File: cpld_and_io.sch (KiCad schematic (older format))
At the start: 3 parts, among them U12 IS61LV5128AL-10TLI, U4 5M1270ZT144C5N

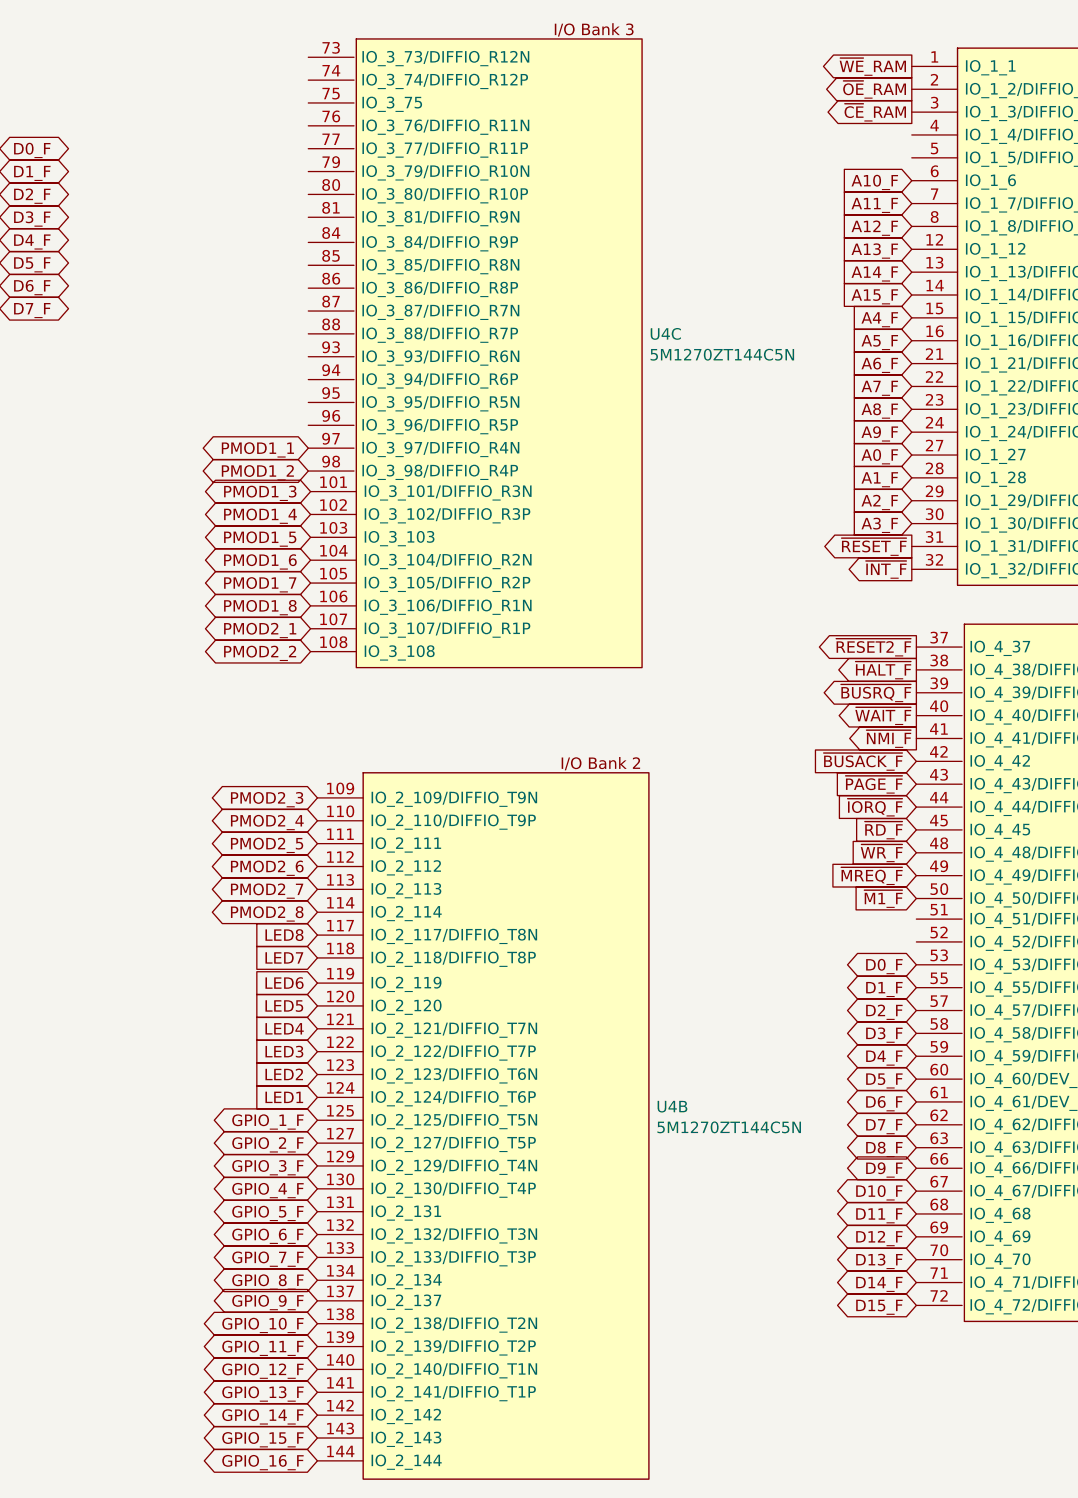
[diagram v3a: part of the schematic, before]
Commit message: organized bypass caps
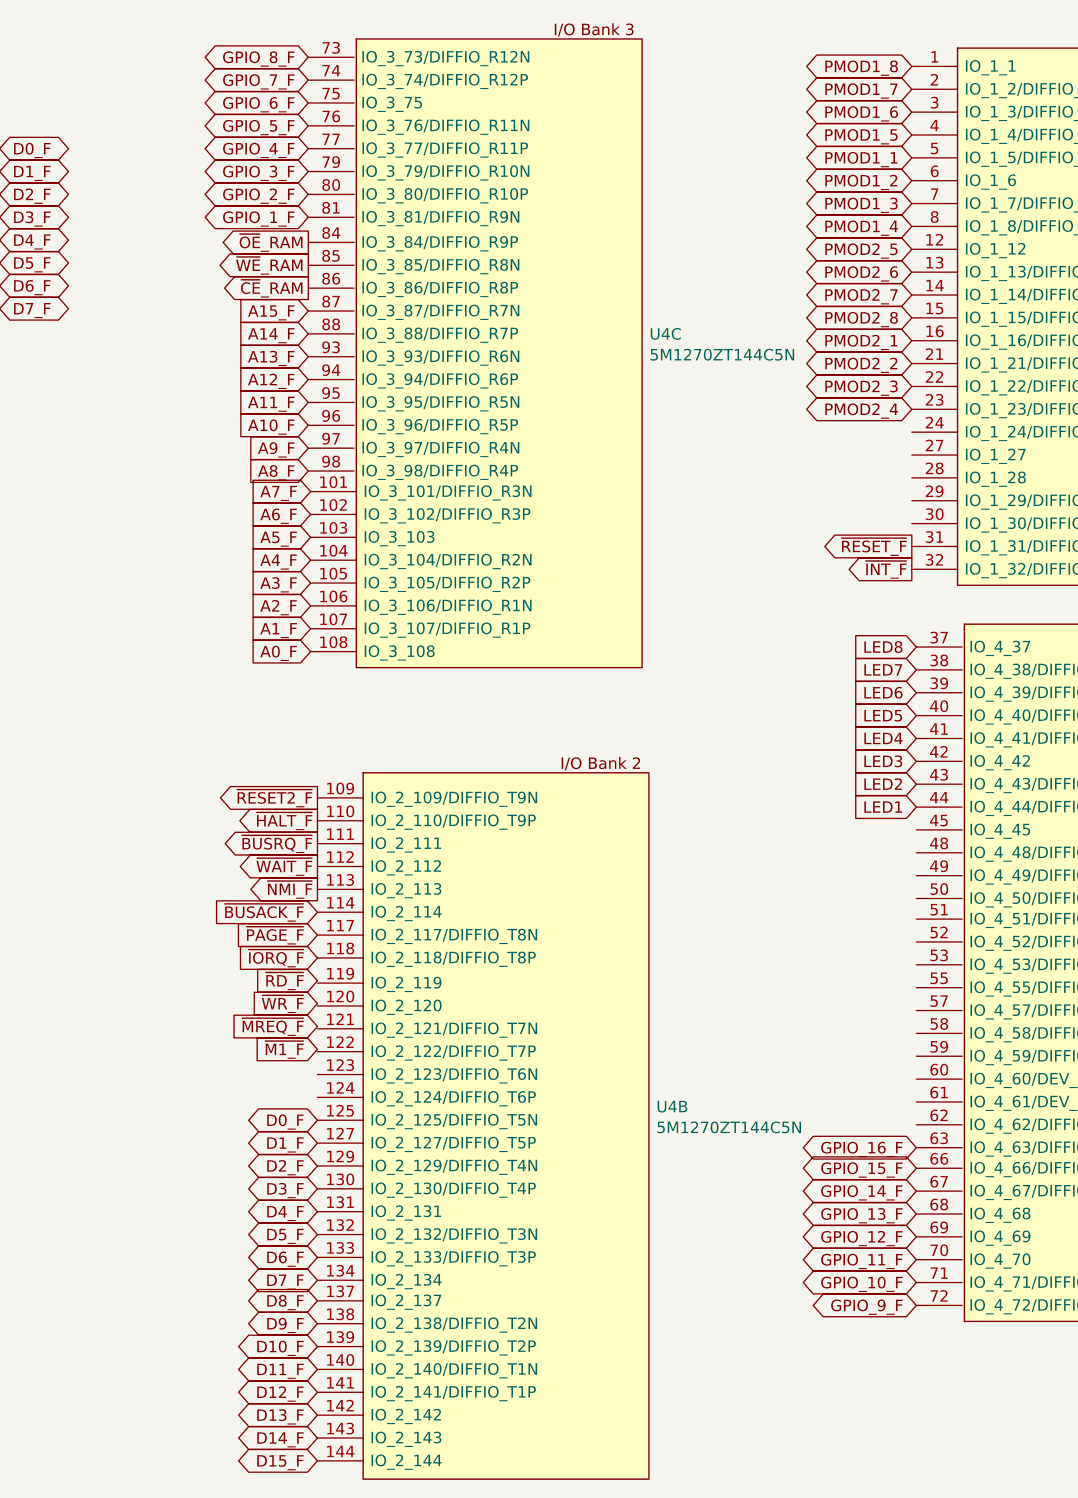
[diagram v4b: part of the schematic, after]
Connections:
- net A0_F: now also U4.108 (IO_3_108); no longer U4.27 (IO_1_27)
- net A10_F: now also U4.96 (IO_3_96/DIFFIO_R5P); no longer U4.6 (IO_1_6)
- net A11_F: now also U4.95 (IO_3_95/DIFFIO_R5N); no longer U4.7 (IO_1_7/DIFFIO_L3P)
- net A12_F: now also U4.94 (IO_3_94/DIFFIO_R6P); no longer U4.8 (IO_1_8/DIFFIO_L3N)
- net A13_F: now also U4.93 (IO_3_93/DIFFIO_R6N); no longer U4.12 (IO_1_12)
- net A14_F: now also U4.88 (IO_3_88/DIFFIO_R7P); no longer U4.13 (IO_1_13/DIFFIO_L4P)
- net A15_F: now also U4.87 (IO_3_87/DIFFIO_R7N); no longer U4.14 (IO_1_14/DIFFIO_L4N)
- net A1_F: now also U4.107 (IO_3_107/DIFFIO_R1P); no longer U4.28 (IO_1_28)
- net A2_F: now also U4.106 (IO_3_106/DIFFIO_R1N); no longer U4.29 (IO_1_29/DIFFIO_L8P)
- net A3_F: now also U4.105 (IO_3_105/DIFFIO_R2P); no longer U4.30 (IO_1_30/DIFFIO_L8N)
- net A4_F: now also U4.104 (IO_3_104/DIFFIO_R2N); no longer U4.15 (IO_1_15/DIFFIO_L5P)
- net A5_F: now also U4.103 (IO_3_103); no longer U4.16 (IO_1_16/DIFFIO_L5N)
- net A6_F: now also U4.102 (IO_3_102/DIFFIO_R3P); no longer U4.21 (IO_1_21/DIFFIO_L6P)
- net A7_F: now also U4.101 (IO_3_101/DIFFIO_R3N); no longer U4.22 (IO_1_22/DIFFIO_L6N)
- net A8_F: now also U4.98 (IO_3_98/DIFFIO_R4P); no longer U4.23 (IO_1_23/DIFFIO_L7P)
- net A9_F: now also U4.97 (IO_3_97/DIFFIO_R4N); no longer U4.24 (IO_1_24/DIFFIO_L7N)
- net D0_F: now also U4.125 (IO_2_125/DIFFIO_T5N); no longer U4.53 (IO_4_53/DIFFIO_B6N)
- net D10_F: now also U4.139 (IO_2_139/DIFFIO_T2P); no longer U4.67 (IO_4_67/DIFFIO_B11N)
- net D11_F: now also U4.140 (IO_2_140/DIFFIO_T1N); no longer U4.68 (IO_4_68)
- net D12_F: now also U4.141 (IO_2_141/DIFFIO_T1P); no longer U4.69 (IO_4_69)
- net D13_F: now also U4.142 (IO_2_142); no longer U4.70 (IO_4_70)
- net D14_F: now also U4.143 (IO_2_143); no longer U4.71 (IO_4_71/DIFFIO_B12P)
- net D15_F: now also U4.144 (IO_2_144); no longer U4.72 (IO_4_72/DIFFIO_B12N)
- net D1_F: now also U4.127 (IO_2_127/DIFFIO_T5P); no longer U4.55 (IO_4_55/DIFFIO_B7P)
- net D2_F: now also U4.129 (IO_2_129/DIFFIO_T4N); no longer U4.57 (IO_4_57/DIFFIO_B7N)
- net D3_F: now also U4.130 (IO_2_130/DIFFIO_T4P); no longer U4.58 (IO_4_58/DIFFIO_B8P)
- net D4_F: now also U4.131 (IO_2_131); no longer U4.59 (IO_4_59/DIFFIO_B8N)
- net D5_F: now also U4.132 (IO_2_132/DIFFIO_T3N); no longer U4.60 (IO_4_60/DEV_OE/DIFFIO_B9P)
- net D6_F: now also U4.133 (IO_2_133/DIFFIO_T3P); no longer U4.61 (IO_4_61/DEV_CLRN/DIFFIO_B9N)
- net D7_F: now also U4.134 (IO_2_134); no longer U4.62 (IO_4_62/DIFFIO_B10P)
- net D8_F: now also U4.137 (IO_2_137); no longer U4.63 (IO_4_63/DIFFIO_B10N)
- net D9_F: now also U4.138 (IO_2_138/DIFFIO_T2N); no longer U4.66 (IO_4_66/DIFFIO_B11P)
- net GPIO_10_F: now also U4.71 (IO_4_71/DIFFIO_B12P); no longer U4.138 (IO_2_138/DIFFIO_T2N)
- net GPIO_11_F: now also U4.70 (IO_4_70); no longer U4.139 (IO_2_139/DIFFIO_T2P)
- net GPIO_12_F: now also U4.69 (IO_4_69); no longer U4.140 (IO_2_140/DIFFIO_T1N)
- net GPIO_13_F: now also U4.68 (IO_4_68); no longer U4.141 (IO_2_141/DIFFIO_T1P)
- net GPIO_14_F: now also U4.67 (IO_4_67/DIFFIO_B11N); no longer U4.142 (IO_2_142)
- net GPIO_15_F: now also U4.66 (IO_4_66/DIFFIO_B11P); no longer U4.143 (IO_2_143)
- net GPIO_16_F: now also U4.63 (IO_4_63/DIFFIO_B10N); no longer U4.144 (IO_2_144)
- net GPIO_1_F: now also U4.81 (IO_3_81/DIFFIO_R9N); no longer U4.125 (IO_2_125/DIFFIO_T5N)
- net GPIO_2_F: now also U4.80 (IO_3_80/DIFFIO_R10P); no longer U4.127 (IO_2_127/DIFFIO_T5P)
- net GPIO_3_F: now also U4.79 (IO_3_79/DIFFIO_R10N); no longer U4.129 (IO_2_129/DIFFIO_T4N)
- net GPIO_4_F: now also U4.77 (IO_3_77/DIFFIO_R11P); no longer U4.130 (IO_2_130/DIFFIO_T4P)
- net GPIO_5_F: now also U4.76 (IO_3_76/DIFFIO_R11N); no longer U4.131 (IO_2_131)
- net GPIO_6_F: now also U4.75 (IO_3_75); no longer U4.132 (IO_2_132/DIFFIO_T3N)
- net GPIO_7_F: now also U4.74 (IO_3_74/DIFFIO_R12P); no longer U4.133 (IO_2_133/DIFFIO_T3P)
- net GPIO_8_F: now also U4.73 (IO_3_73/DIFFIO_R12N); no longer U4.134 (IO_2_134)
- net GPIO_9_F: now also U4.72 (IO_4_72/DIFFIO_B12N); no longer U4.137 (IO_2_137)
- net LED1: now also U4.44 (IO_4_44/DIFFIO_B3N); no longer U4.124 (IO_2_124/DIFFIO_T6P)
- net LED2: now also U4.43 (IO_4_43/DIFFIO_B3P); no longer U4.123 (IO_2_123/DIFFIO_T6N)
- net LED3: now also U4.42 (IO_4_42); no longer U4.122 (IO_2_122/DIFFIO_T7P)
- net LED4: now also U4.41 (IO_4_41/DIFFIO_B2N); no longer U4.121 (IO_2_121/DIFFIO_T7N)
- net LED5: now also U4.40 (IO_4_40/DIFFIO_B2P); no longer U4.120 (IO_2_120)
- net LED6: now also U4.39 (IO_4_39/DIFFIO_B1N); no longer U4.119 (IO_2_119)
- net LED7: now also U4.38 (IO_4_38/DIFFIO_B1P); no longer U4.118 (IO_2_118/DIFFIO_T8P)
- net LED8: now also U4.37 (IO_4_37); no longer U4.117 (IO_2_117/DIFFIO_T8N)
- net PMOD1_1: now also U4.5 (IO_1_5/DIFFIO_L2N); no longer U4.97 (IO_3_97/DIFFIO_R4N)
- net PMOD1_2: now also U4.6 (IO_1_6); no longer U4.98 (IO_3_98/DIFFIO_R4P)
- net PMOD1_3: now also U4.7 (IO_1_7/DIFFIO_L3P); no longer U4.101 (IO_3_101/DIFFIO_R3N)
- net PMOD1_4: now also U4.8 (IO_1_8/DIFFIO_L3N); no longer U4.102 (IO_3_102/DIFFIO_R3P)
- net PMOD1_5: now also U4.4 (IO_1_4/DIFFIO_L2P); no longer U4.103 (IO_3_103)
- net PMOD1_6: now also U4.3 (IO_1_3/DIFFIO_L1N); no longer U4.104 (IO_3_104/DIFFIO_R2N)
- net PMOD1_7: now also U4.2 (IO_1_2/DIFFIO_L1P); no longer U4.105 (IO_3_105/DIFFIO_R2P)
- net PMOD1_8: now also U4.1 (IO_1_1); no longer U4.106 (IO_3_106/DIFFIO_R1N)
- net PMOD2_1: now also U4.16 (IO_1_16/DIFFIO_L5N); no longer U4.107 (IO_3_107/DIFFIO_R1P)
- net PMOD2_2: now also U4.21 (IO_1_21/DIFFIO_L6P); no longer U4.108 (IO_3_108)
- net PMOD2_3: now also U4.22 (IO_1_22/DIFFIO_L6N); no longer U4.109 (IO_2_109/DIFFIO_T9N)
- net PMOD2_4: now also U4.23 (IO_1_23/DIFFIO_L7P); no longer U4.110 (IO_2_110/DIFFIO_T9P)
- net PMOD2_5: now also U4.12 (IO_1_12); no longer U4.111 (IO_2_111)
- net PMOD2_6: now also U4.13 (IO_1_13/DIFFIO_L4P); no longer U4.112 (IO_2_112)
- net PMOD2_7: now also U4.14 (IO_1_14/DIFFIO_L4N); no longer U4.113 (IO_2_113)
- net PMOD2_8: now also U4.15 (IO_1_15/DIFFIO_L5P); no longer U4.114 (IO_2_114)
- net ~BUSACK_F: now also U4.114 (IO_2_114); no longer U4.42 (IO_4_42)
- net ~BUSRQ_F: now also U4.111 (IO_2_111); no longer U4.39 (IO_4_39/DIFFIO_B1N)
- net ~CE~_RAM: now also U4.86 (IO_3_86/DIFFIO_R8P); no longer U4.3 (IO_1_3/DIFFIO_L1N)
- net ~HALT_F: now also U4.110 (IO_2_110/DIFFIO_T9P); no longer U4.38 (IO_4_38/DIFFIO_B1P)
- net ~IORQ_F: now also U4.118 (IO_2_118/DIFFIO_T8P); no longer U4.44 (IO_4_44/DIFFIO_B3N)
- net ~M1_F: no longer U4.50 (IO_4_50/DIFFIO_B5P)
- net ~MREQ_F: no longer U4.49 (IO_4_49/DIFFIO_B4N)
- net ~NMI_F: now also U4.113 (IO_2_113); no longer U4.41 (IO_4_41/DIFFIO_B2N)
- net ~OE~_RAM: now also U4.84 (IO_3_84/DIFFIO_R9P); no longer U4.2 (IO_1_2/DIFFIO_L1P)
- net ~PAGE_F: now also U4.117 (IO_2_117/DIFFIO_T8N); no longer U4.43 (IO_4_43/DIFFIO_B3P)
- net ~RD_F: no longer U4.45 (IO_4_45)
- net ~RESET2_F: now also U4.109 (IO_2_109/DIFFIO_T9N); no longer U4.37 (IO_4_37)
- net ~WAIT_F: now also U4.112 (IO_2_112); no longer U4.40 (IO_4_40/DIFFIO_B2P)
- net ~WE~_RAM: now also U4.85 (IO_3_85/DIFFIO_R8N); no longer U4.1 (IO_1_1)
- net ~WR_F: no longer U4.48 (IO_4_48/DIFFIO_B4P)
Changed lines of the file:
@@
 NoConn ~ 1830 2850
 NoConn ~ 1830 2950
-Text GLabel 7020 1490 0    50   Input ~ 0
-A12_F
-Text GLabel 7020 1590 0    50   Input ~ 0
-A13_F
-Text GLabel 7020 1690 0    50   Input ~ 0
-A14_F
-Text GLabel 7020 1790 0    50   Input ~ 0
-A15_F
-Text GLabel 7020 1390 0    50   Input ~ 0
-A11_F
-Text GLabel 7020 1290 0    50   Input ~ 0
-A10_F
-Text GLabel 7020 2390 0    50   Input ~ 0
+Text GLabel 4380 2460 0    50   Input ~ 0
 A9_F
-Text GLabel 7020 2290 0    50   Input ~ 0
+Text GLabel 4380 2560 0    50   Input ~ 0
 A8_F
-Text GLabel 7020 2190 0    50   Input ~ 0
+Text GLabel 4390 2650 0    50   Input ~ 0
 A7_F
-Text GLabel 7020 2090 0    50   Input ~ 0
+Text GLabel 4390 2750 0    50   Input ~ 0
 A6_F
-Text GLabel 7020 1990 0    50   Input ~ 0
+Text GLabel 4390 2850 0    50   Input ~ 0
 A5_F
-Text GLabel 7020 1890 0    50   Input ~ 0
+Text GLabel 4390 2950 0    50   Input ~ 0
 A4_F
-Text GLabel 7020 2790 0    50   Input ~ 0
+Text GLabel 4390 3050 0    50   Input ~ 0
 A3_F
-Text GLabel 7020 2690 0    50   Input ~ 0
+Text GLabel 4390 3150 0    50   Input ~ 0
 A2_F
-Text GLabel 7020 2590 0    50   Input ~ 0
+Text GLabel 4390 3250 0    50   Input ~ 0
 A1_F
-Text GLabel 7020 2490 0    50   Input ~ 0
+Text GLabel 4390 3350 0    50   Input ~ 0
 A0_F
-Text GLabel 7040 5420 0    50   3State ~ 0
+Text GLabel 4420 6100 0    50   3State ~ 0
 D7_F
-Text GLabel 7040 5320 0    50   3State ~ 0
+Text GLabel 4420 6000 0    50   3State ~ 0
 D6_F
-Text GLabel 7040 5220 0    50   3State ~ 0
+Text GLabel 4420 5900 0    50   3State ~ 0
 D5_F
-Text GLabel 7040 5120 0    50   3State ~ 0
+Text GLabel 4420 5800 0    50   3State ~ 0
 D4_F
-Text GLabel 7040 5020 0    50   3State ~ 0
+Text GLabel 4420 5700 0    50   3State ~ 0
 D3_F
-Text GLabel 7040 4920 0    50   3State ~ 0
+Text GLabel 4420 5600 0    50   3State ~ 0
 D2_F
-Text GLabel 7040 4820 0    50   3State ~ 0
+Text GLabel 4420 5500 0    50   3State ~ 0
 D1_F
-Text GLabel 7040 4720 0    50   3State ~ 0
+Text GLabel 4420 5400 0    50   3State ~ 0
 D0_F
-Text GLabel 7040 3830 0    50   Input ~ 0
+Text GLabel 4420 4490 0    50   Input ~ 0
 ~BUSACK_F
-Text GLabel 7040 3930 0    50   Input ~ 0
+Text GLabel 4420 4590 0    50   Input ~ 0
 ~PAGE_F
-Text GLabel 7040 4330 0    50   Input ~ 0
+Text GLabel 4420 4990 0    50   Input ~ 0
 ~MREQ_F
-Text GLabel 7040 4230 0    50   Input ~ 0
+Text GLabel 4420 4890 0    50   Input ~ 0
 ~WR_F
-Text GLabel 7040 4130 0    50   Input ~ 0
+Text GLabel 4420 4790 0    50   Input ~ 0
 ~RD_F
-Text GLabel 7040 4030 0    50   Input ~ 0
+Text GLabel 4420 4690 0    50   Input ~ 0
 ~IORQ_F
-Text GLabel 7040 4430 0    50   Input ~ 0
+Text GLabel 4420 5090 0    50   Input ~ 0
 ~M1_F
-Text GLabel 7040 3430 0    50   Output ~ 0
+Text GLabel 4420 4090 0    50   Output ~ 0
 ~HALT_F
-Text GLabel 7040 3530 0    50   Output ~ 0
+Text GLabel 4420 4190 0    50   Output ~ 0
 ~BUSRQ_F
-Text GLabel 7040 3630 0    50   Output ~ 0
+Text GLabel 4420 4290 0    50   Output ~ 0
 ~WAIT_F
-Text GLabel 7040 3730 0    50   Output ~ 0
+Text GLabel 4420 4390 0    50   Output ~ 0
 ~NMI_F
-Text GLabel 7040 3330 0    50   Output ~ 0
+Text GLabel 4420 3990 0    50   Output ~ 0
 ~RESET2_F
 Text GLabel 7020 2990 0    50   Output ~ 0
@@
 Text GLabel 7020 2890 0    50   Output ~ 0
 ~RESET_F
-Text GLabel 7040 6210 0    50   3State ~ 0
+Text GLabel 4420 6890 0    50   3State ~ 0
 D15_F
-Text GLabel 7040 6110 0    50   3State ~ 0
+Text GLabel 4420 6790 0    50   3State ~ 0
 D14_F
-Text GLabel 7040 6010 0    50   3State ~ 0
+Text GLabel 4420 6690 0    50   3State ~ 0
 D13_F
-Text GLabel 7040 5910 0    50   3State ~ 0
+Text GLabel 4420 6590 0    50   3State ~ 0
 D12_F
-Text GLabel 7040 5810 0    50   3State ~ 0
+Text GLabel 4420 6490 0    50   3State ~ 0
 D11_F
-Text GLabel 7040 5710 0    50   3State ~ 0
+Text GLabel 4420 6390 0    50   3State ~ 0
 D10_F
-Text GLabel 7040 5610 0    50   3State ~ 0
+Text GLabel 4420 6290 0    50   3State ~ 0
 D9_F
-Text GLabel 7040 5520 0    50   3State ~ 0
+Text GLabel 4420 6190 0    50   3State ~ 0
 D8_F
-Text GLabel 7020 790  0    50   Output ~ 0
-~WE~_RAM
-Text GLabel 7020 890  0    50   Output ~ 0
-~OE~_RAM
-Text GLabel 7020 990  0    50   Output ~ 0
+Text GLabel 4380 1760 0    50   Output ~ 0
 ~CE~_RAM
 $Comp
@@
 	1    0    0    -1
 $EndComp
-Text GLabel 4420 6100 0    50   3State ~ 0
-GPIO_8_F
-Text GLabel 4420 6000 0    50   3State ~ 0
-GPIO_7_F
-Text GLabel 4420 5900 0    50   3State ~ 0
-GPIO_6_F
-Text GLabel 4420 5800 0    50   3State ~ 0
-GPIO_5_F
-Text GLabel 4420 5700 0    50   3State ~ 0
-GPIO_4_F
-Text GLabel 4420 5600 0    50   3State ~ 0
-GPIO_3_F
-Text GLabel 4420 5500 0    50   3State ~ 0
-GPIO_2_F
-Text GLabel 4420 5400 0    50   3State ~ 0
-GPIO_1_F
-Text GLabel 4420 6890 0    50   3State ~ 0
-GPIO_16_F
-Text GLabel 4420 6790 0    50   3State ~ 0
-GPIO_15_F
-Text GLabel 4420 6690 0    50   3State ~ 0
-GPIO_14_F
-Text GLabel 4420 6590 0    50   3State ~ 0
-GPIO_13_F
-Text GLabel 4420 6490 0    50   3State ~ 0
-GPIO_12_F
-Text GLabel 4420 6390 0    50   3State ~ 0
-GPIO_11_F
-Text GLabel 4420 6290 0    50   3State ~ 0
+Text GLabel 7040 6110 0    50   3State ~ 0
 GPIO_10_F
-Text GLabel 4420 6190 0    50   3State ~ 0
+Text GLabel 7040 6210 0    50   3State ~ 0
 GPIO_9_F
 Text GLabel 1000 3250 0    50   Input ~ 0
@@
 	1310 3350 1000 3350
 NoConn ~ 1410 2980
-Text GLabel 4380 2460 0    50   3State ~ 0
+Text GLabel 7020 1190 0    50   3State ~ 0
 PMOD1_1
-Text GLabel 4380 2560 0    50   3State ~ 0
+Text GLabel 7020 1290 0    50   3State ~ 0
 PMOD1_2
-Text GLabel 4390 2650 0    50   3State ~ 0
+Text GLabel 7020 1390 0    50   3State ~ 0
 PMOD1_3
-Text GLabel 4390 2750 0    50   3State ~ 0
+Text GLabel 7020 1490 0    50   3State ~ 0
 PMOD1_4
-Text GLabel 4390 2850 0    50   3State ~ 0
+Text GLabel 7020 1090 0    50   3State ~ 0
 PMOD1_5
-Text GLabel 4390 2950 0    50   3State ~ 0
+Text GLabel 7020 990  0    50   3State ~ 0
 PMOD1_6
-Text GLabel 4390 3050 0    50   3State ~ 0
+Text GLabel 7020 890  0    50   3State ~ 0
 PMOD1_7
-Text GLabel 4390 3150 0    50   3State ~ 0
+Text GLabel 7020 790  0    50   3State ~ 0
 PMOD1_8
-Text GLabel 4390 3250 0    50   3State ~ 0
+Text GLabel 7020 1990 0    50   3State ~ 0
 PMOD2_1
-Text GLabel 4390 3350 0    50   3State ~ 0
+Text GLabel 7020 2090 0    50   3State ~ 0
 PMOD2_2
-Text GLabel 4420 3990 0    50   3State ~ 0
+Text GLabel 7020 2190 0    50   3State ~ 0
 PMOD2_3
-Text GLabel 4420 4090 0    50   3State ~ 0
+Text GLabel 7020 2290 0    50   3State ~ 0
 PMOD2_4
-Text GLabel 4420 4490 0    50   3State ~ 0
+Text GLabel 7020 1890 0    50   3State ~ 0
 PMOD2_8
-Text GLabel 4420 4390 0    50   3State ~ 0
+Text GLabel 7020 1790 0    50   3State ~ 0
 PMOD2_7
-Text GLabel 4420 4290 0    50   3State ~ 0
+Text GLabel 7020 1690 0    50   3State ~ 0
 PMOD2_6
-Text GLabel 4420 4190 0    50   3State ~ 0
+Text GLabel 7020 1590 0    50   3State ~ 0
 PMOD2_5
-Text GLabel 4420 5000 0    50   Input ~ 0
+Text GLabel 7040 3730 0    50   Input ~ 0
 LED4
-Text GLabel 4420 4900 0    50   Input ~ 0
+Text GLabel 7040 3630 0    50   Input ~ 0
 LED5
-Text GLabel 4420 4800 0    50   Input ~ 0
+Text GLabel 7040 3530 0    50   Input ~ 0
 LED6
-Text GLabel 4420 4690 0    50   Input ~ 0
+Text GLabel 7040 3430 0    50   Input ~ 0
 LED7
-Text GLabel 4420 4590 0    50   Input ~ 0
+Text GLabel 7040 3330 0    50   Input ~ 0
 LED8
-Text GLabel 4420 5100 0    50   Input ~ 0
+Text GLabel 7040 3830 0    50   Input ~ 0
 LED3
-Text GLabel 4420 5200 0    50   Input ~ 0
+Text GLabel 7040 3930 0    50   Input ~ 0
 LED2
-Text GLabel 4420 5300 0    50   Input ~ 0
+Text GLabel 7040 4030 0    50   Input ~ 0
 LED1
 $Sheet
@@
 F1 "clocks.sch" 50
 $EndSheet
+Text GLabel 4380 1350 0    50   3State ~ 0
+GPIO_2_F
+Text GLabel 4380 1250 0    50   3State ~ 0
+GPIO_3_F
+Text GLabel 4380 1150 0    50   3State ~ 0
+GPIO_4_F
+Text GLabel 4380 1050 0    50   3State ~ 0
+GPIO_5_F
+Text GLabel 4380 950  0    50   3State ~ 0
+GPIO_6_F
+Text GLabel 4380 850  0    50   3State ~ 0
+GPIO_7_F
+Text GLabel 4380 750  0    50   3State ~ 0
+GPIO_8_F
+Text GLabel 7040 6010 0    50   3State ~ 0
+GPIO_11_F
+Text GLabel 7040 5910 0    50   3State ~ 0
+GPIO_12_F
+Text GLabel 7040 5810 0    50   3State ~ 0
+GPIO_13_F
+Text GLabel 7040 5710 0    50   3State ~ 0
+GPIO_14_F
+Text GLabel 7040 5610 0    50   3State ~ 0
+GPIO_15_F
+Text GLabel 7040 5520 0    50   3State ~ 0
+GPIO_16_F
+Text GLabel 4380 2360 0    50   Input ~ 0
+A10_F
+Text GLabel 4380 2260 0    50   Input ~ 0
+A11_F
+Text GLabel 4380 1860 0    50   Input ~ 0
+A15_F
+Text GLabel 4380 1960 0    50   Input ~ 0
+A14_F
+Text GLabel 4380 2060 0    50   Input ~ 0
+A13_F
+Text GLabel 4380 2160 0    50   Input ~ 0
+A12_F
+Text GLabel 4380 1450 0    50   3State ~ 0
+GPIO_1_F
+Text GLabel 4380 1560 0    50   Output ~ 0
+~OE~_RAM
+Text GLabel 4380 1660 0    50   Output ~ 0
+~WE~_RAM
 $EndSCHEMATC
